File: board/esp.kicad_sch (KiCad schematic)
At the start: 5 parts, among them U1 ESP32-S3-WROOM-1

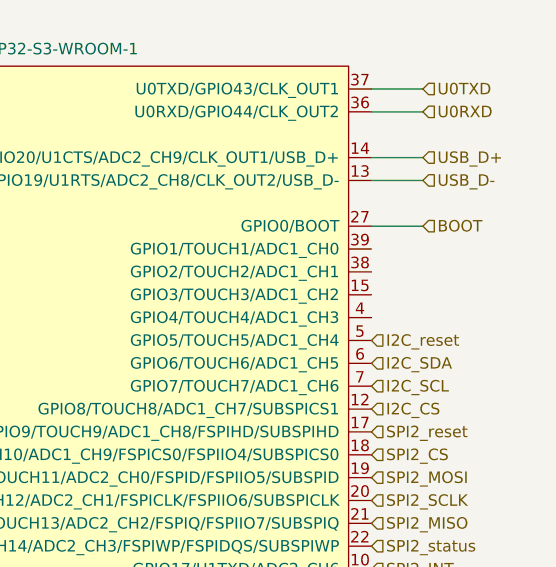
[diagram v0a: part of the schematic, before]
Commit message: added usb and ADC connectors
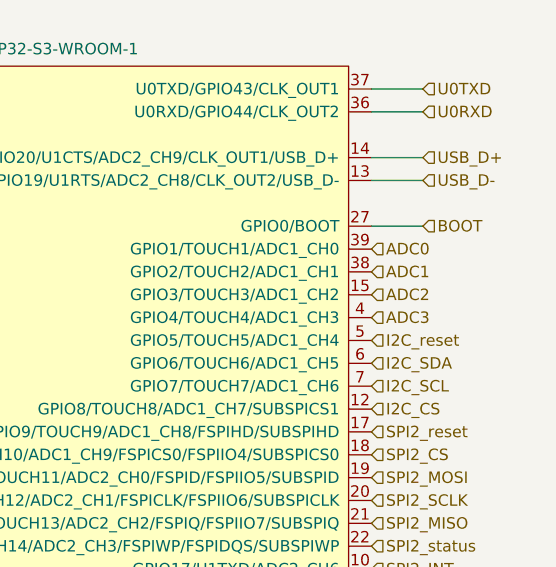
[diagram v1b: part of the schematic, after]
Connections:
- net ADC2: now reaches U1.15 (GPIO3/TOUCH3/ADC1_CH2)
- net ADC1: now reaches U1.38 (GPIO2/TOUCH2/ADC1_CH1)
- net ADC0: now reaches U1.39 (GPIO1/TOUCH1/ADC1_CH0)
- net ADC3: now reaches U1.4 (GPIO4/TOUCH4/ADC1_CH3)
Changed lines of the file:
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@@
+    (effects (font (size 1.27 1.27)) (justify left))
+  )
+  (hierarchical_label "ADC1" (shape input) (at 179.07 83.185 0) (fields_autoplaced)
     (effects (font (size 1.27 1.27)) (justify left))
   )
@@
     (effects (font (size 1.27 1.27)) (justify left))
   )
+  (hierarchical_label "ADC3" (shape input) (at 179.07 88.265 0) (fields_autoplaced)
+    (effects (font (size 1.27 1.27)) (justify left))
+  )
+  (hierarchical_label "ADC2" (shape input) (at 179.07 85.725 0) (fields_autoplaced)
+    (effects (font (size 1.27 1.27)) (justify left))
+  )
+  (hierarchical_label "ADC0" (shape input) (at 179.07 80.645 0) (fields_autoplaced)
+    (effects (font (size 1.27 1.27)) (justify left))
+  )
